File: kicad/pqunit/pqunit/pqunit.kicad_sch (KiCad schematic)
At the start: 15 parts, among them J1 Conn_02x10_PQSU, J2 Conn_01x10, U1 ATMEGA328P-AU, U5 MAX485E, U6 Ai-Thinker-Ra-02, Y1 Crystal

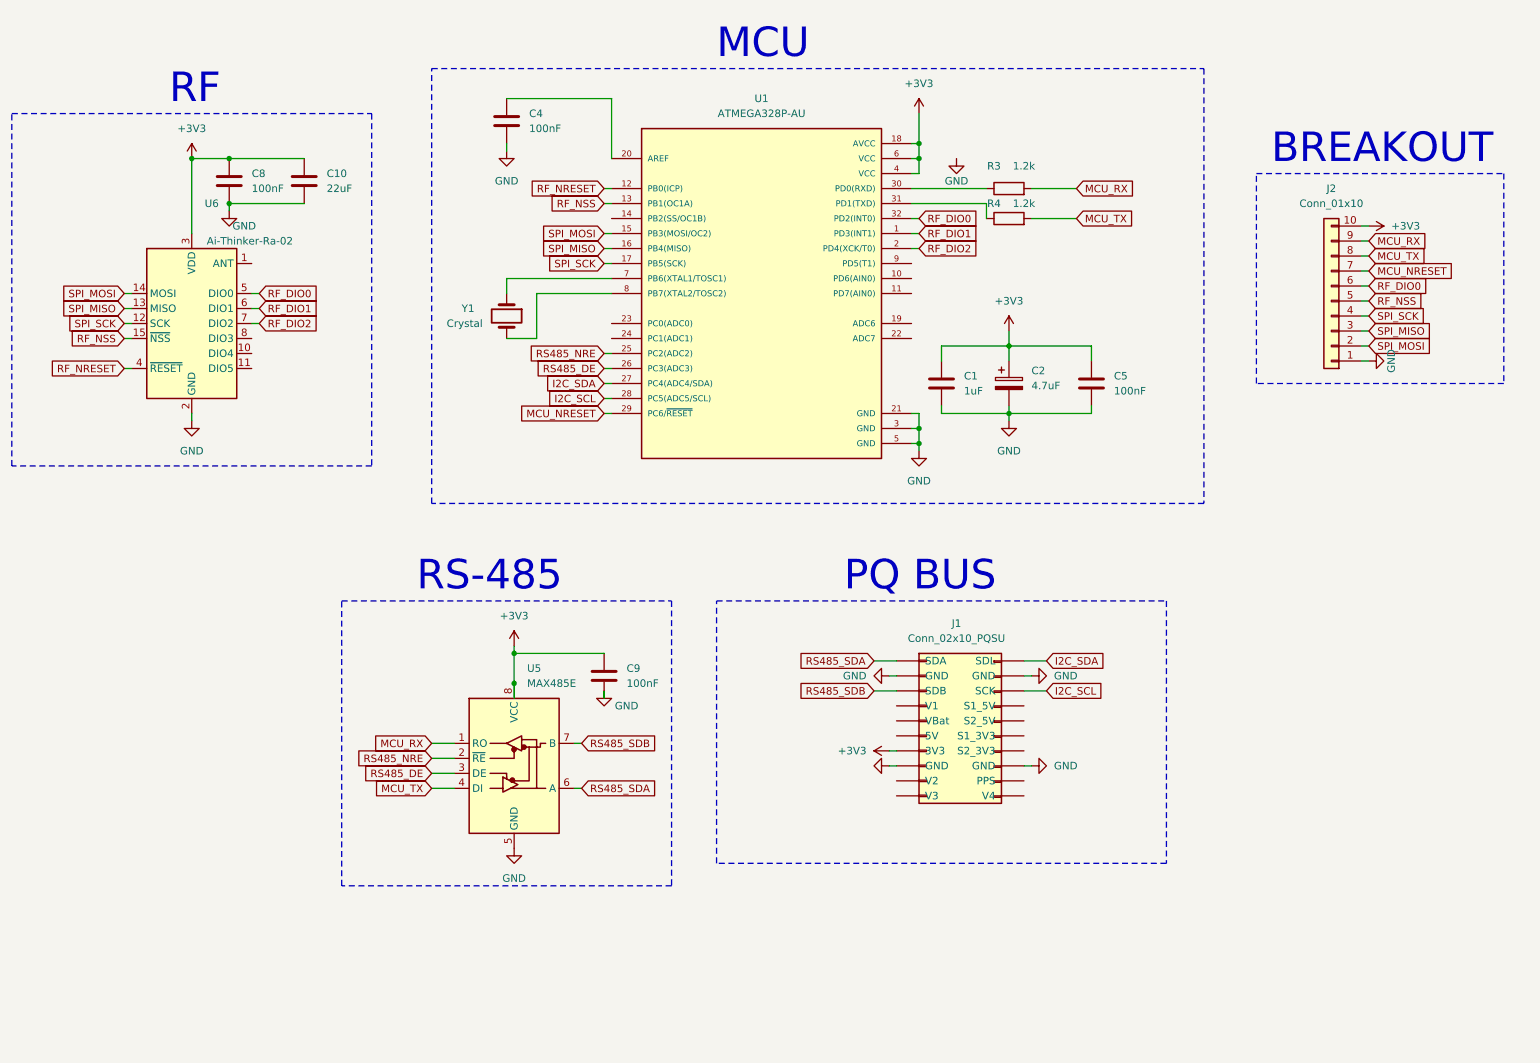
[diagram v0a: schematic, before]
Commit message: Began PQUnit PCB Rev 2
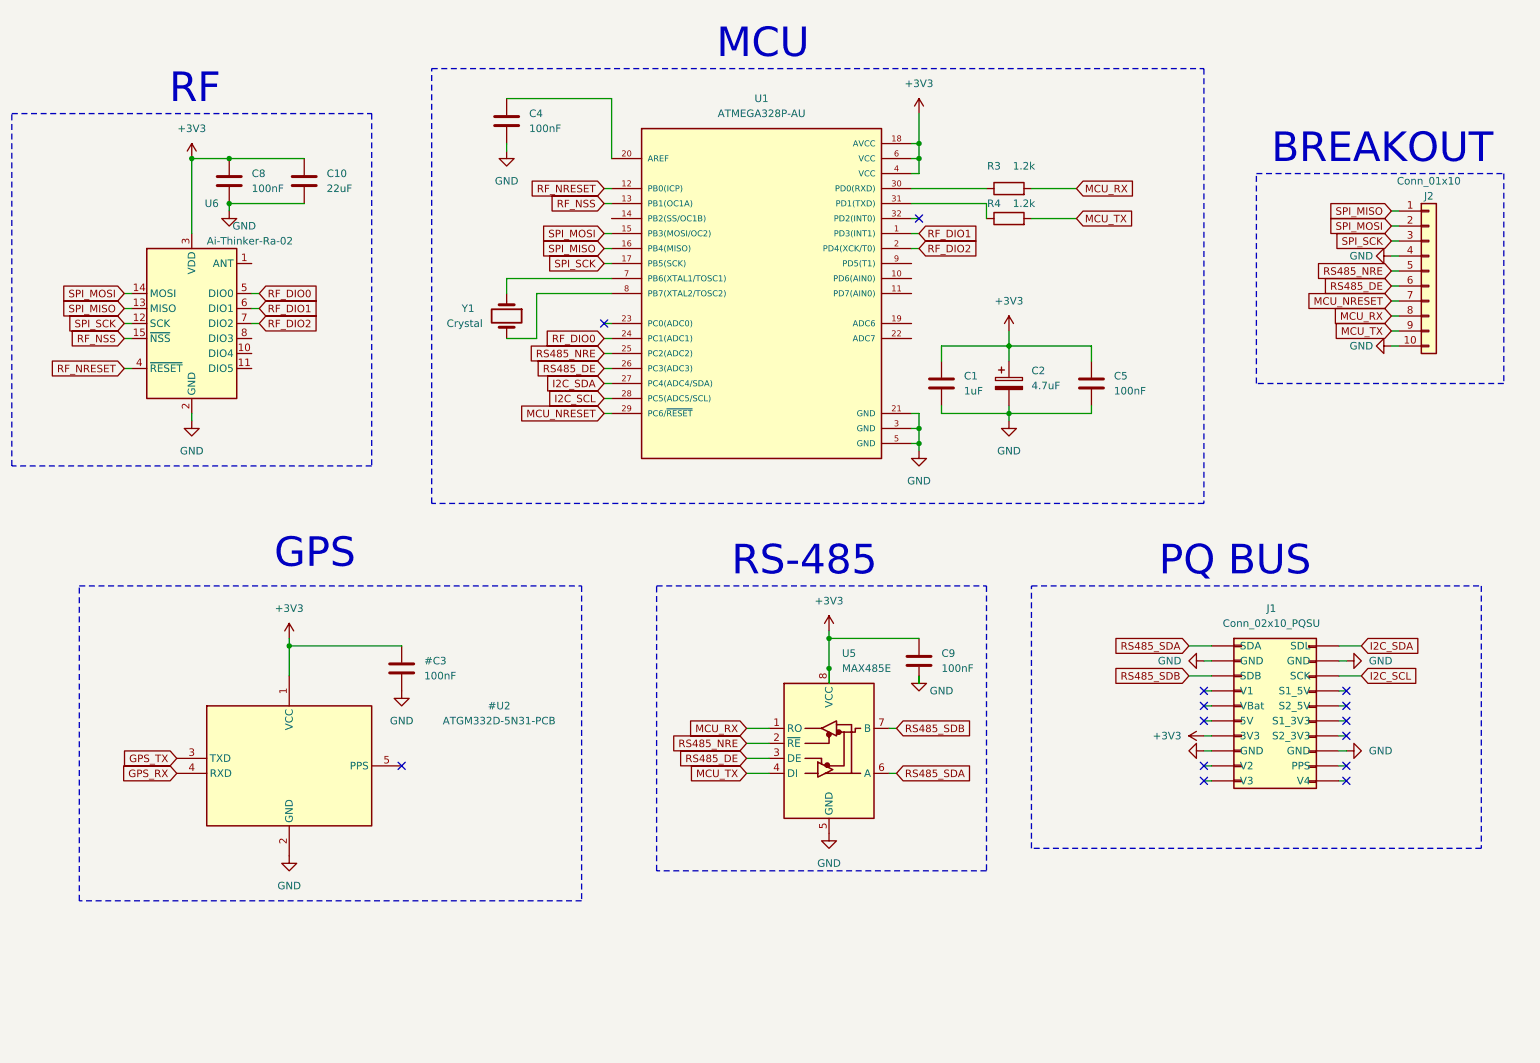
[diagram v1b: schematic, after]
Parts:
- added #C3: 100nF, Capacitor_SMD:C_0603_1608Metric_Pad1.08x0.95mm_HandSolder, symbol Device:C
- added #U2: ATGM332D-5N31-PCB, ATGM332D-5N31-PCB:ATGM332D-5N31-PCB, symbol ATGM332D-5N31-PCB:ATGM332D-5N31
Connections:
- net +3V3: now also #C3.1, #U2.1 (VCC); no longer J2.10 (Pin_10)
- net GND: now also J2.10 (Pin_10), J2.4 (Pin_4), #C3.2, #U2.2 (GND); no longer J2.1 (Pin_1)
- net MCU_RX: now also J2.8 (Pin_8); no longer J2.9 (Pin_9)
- net MCU_TX: now also J2.9 (Pin_9); no longer J2.8 (Pin_8)
- net RF_DIO0: now also U1.24 (PC1(ADC1)); no longer J2.6 (Pin_6), U1.32 (PD2(INT0))
- net RF_NSS: no longer J2.5 (Pin_5)
- net RS485_DE: now also J2.6 (Pin_6)
- net RS485_NRE: now also J2.5 (Pin_5)
- net SPI_MISO: now also J2.1 (Pin_1); no longer J2.3 (Pin_3)
- net SPI_SCK: now also J2.3 (Pin_3); no longer J2.4 (Pin_4)
- new net GPS_RX: #U2.4 (RXD)
- new net GPS_TX: #U2.3 (TXD)
- no-connect marks 0 -> 14
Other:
- note added: "GPS"
- moved on the sheet: C9, J1, J2, U5

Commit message: Finished both PCB latest revisions
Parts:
- added JP1: Jumper_2_Bridged, TestPoint:TestPoint_2Pads_Pitch2.54mm_Drill0.8mm, symbol Jumper:Jumper_2_Bridged
- #C3, C4, C5, C8, C9: footprint Capacitor_SMD:C_0603_1608Metric_Pad1.08x0.95mm_HandSolder -> Capacitor_SMD:C_0805_2012Metric_Pad1.18x1.45mm_HandSolder
- C1, C10: footprint Capacitor_SMD:C_0805_2012Metric_Pad1.18x1.45mm_HandSolder -> Capacitor_SMD:C_1206_3216Metric_Pad1.33x1.80mm_HandSolder
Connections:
- net +3V3: now also J2.9 (Pin_9), JP1.1 (A); no longer J1.7 (3V3)
- net GND: no longer J2.4 (Pin_4)
- net MCU_NRESET: now also J2.6 (Pin_6); no longer J2.7 (Pin_7)
- net MCU_RX: now also J2.7 (Pin_7); no longer J2.8 (Pin_8)
- net MCU_TX: now also J2.8 (Pin_8); no longer J2.9 (Pin_9)
- net RS485_DE: now also J2.5 (Pin_5); no longer J2.6 (Pin_6)
- net RS485_NRE: now also J2.4 (Pin_4); no longer J2.5 (Pin_5)
- new net 3V3_Bus: J1.7 (3V3), JP1.2 (B)

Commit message: Added ISP
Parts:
- removed #C3: 100nF, Capacitor_SMD:C_0805_2012Metric_Pad1.18x1.45mm_HandSolder, symbol Device:C
- removed #U2: ATGM332D-5N31-PCB, ATGM332D-5N31-PCB:ATGM332D-5N31-PCB, symbol ATGM332D-5N31-PCB:ATGM332D-5N31
- removed JP1: Jumper_2_Bridged, TestPoint:TestPoint_2Pads_Pitch2.54mm_Drill0.8mm, symbol Jumper:Jumper_2_Bridged
- added C6: 10uF, Capacitor_SMD:C_1206_3216Metric_Pad1.33x1.80mm_HandSolder, symbol Device:C
- added J3: Conn_Coaxial, Connector_Coaxial:U.FL_Molex_MCRF_73412-0110_Vertical, symbol Connector:Conn_Coaxial
- added U3: ATGM332D-5N31, LIB_ATGM332D-5N31:ATGM332D5N31, symbol ATGM332D-5N31:ATGM332D-5N31
- renumbered U6 to U2, U5 to U4
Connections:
- net 3V3_Bus is gone; now on net +3V3: J1.7 (3V3)
- net +3V3: now also C6.1, U3.22 (VBAT), U3.23 (VCC); no longer J2.9 (Pin_9)
- net GND: now also J2.9 (Pin_9), C6.2, J3.2 (Ext), U3.10 (GND_1), U3.12 (GND_2), U3.13 (GND_3), U3.24 (GND_4)
- net GPS_RX: now also U1.10 (PD6(AIN0)), U3.21 (RXD1)
- net GPS_TX: now also U1.11 (PD7(AIN0)), U3.20 (TXD1)
- new net: J3.1 (In), U3.11 (RF_IN)
- no-connect marks 14 -> 13
